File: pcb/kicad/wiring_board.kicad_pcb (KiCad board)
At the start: 2 copper layers, 47 x 72 mm, 13 parts, among them J1 2604-1106, J2 5V out

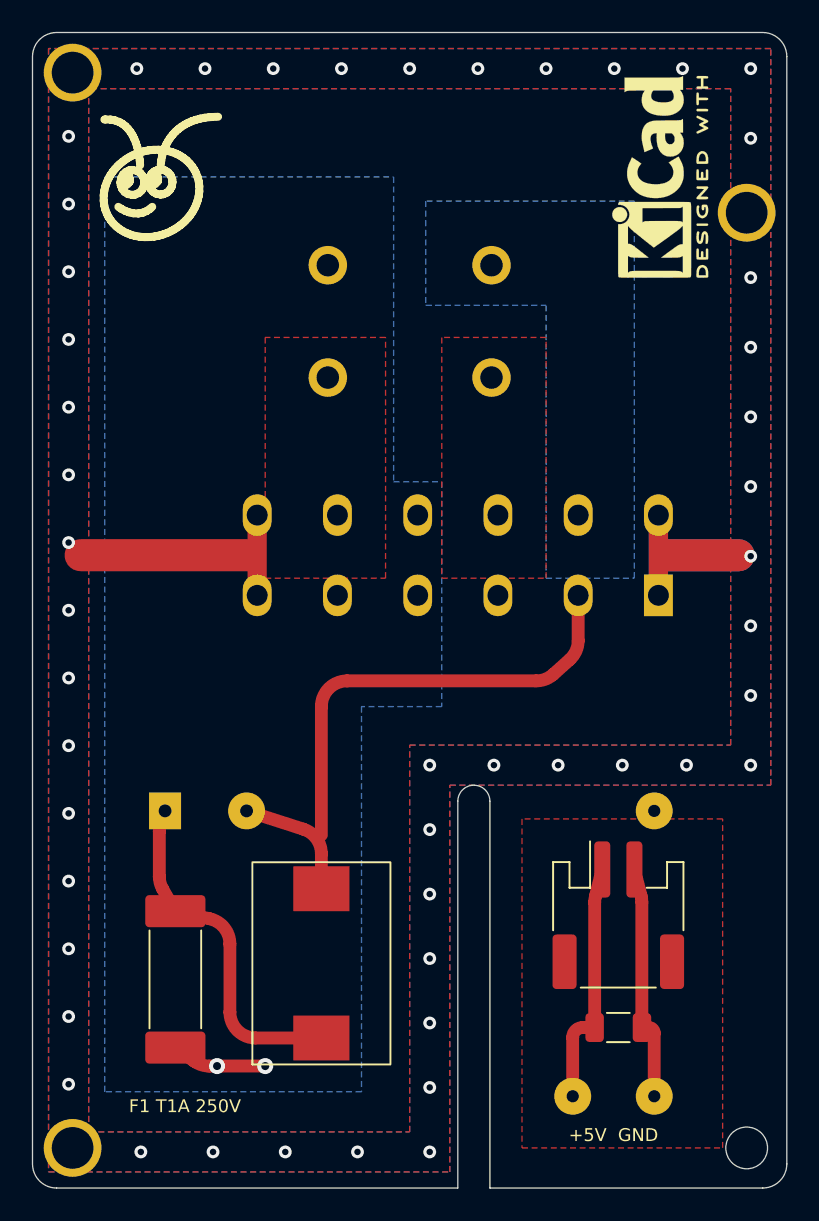
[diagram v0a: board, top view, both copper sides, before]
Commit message: Wiring board: J1 and rocker from vendor models, rocker clear of WAGO pins, LOAD labels
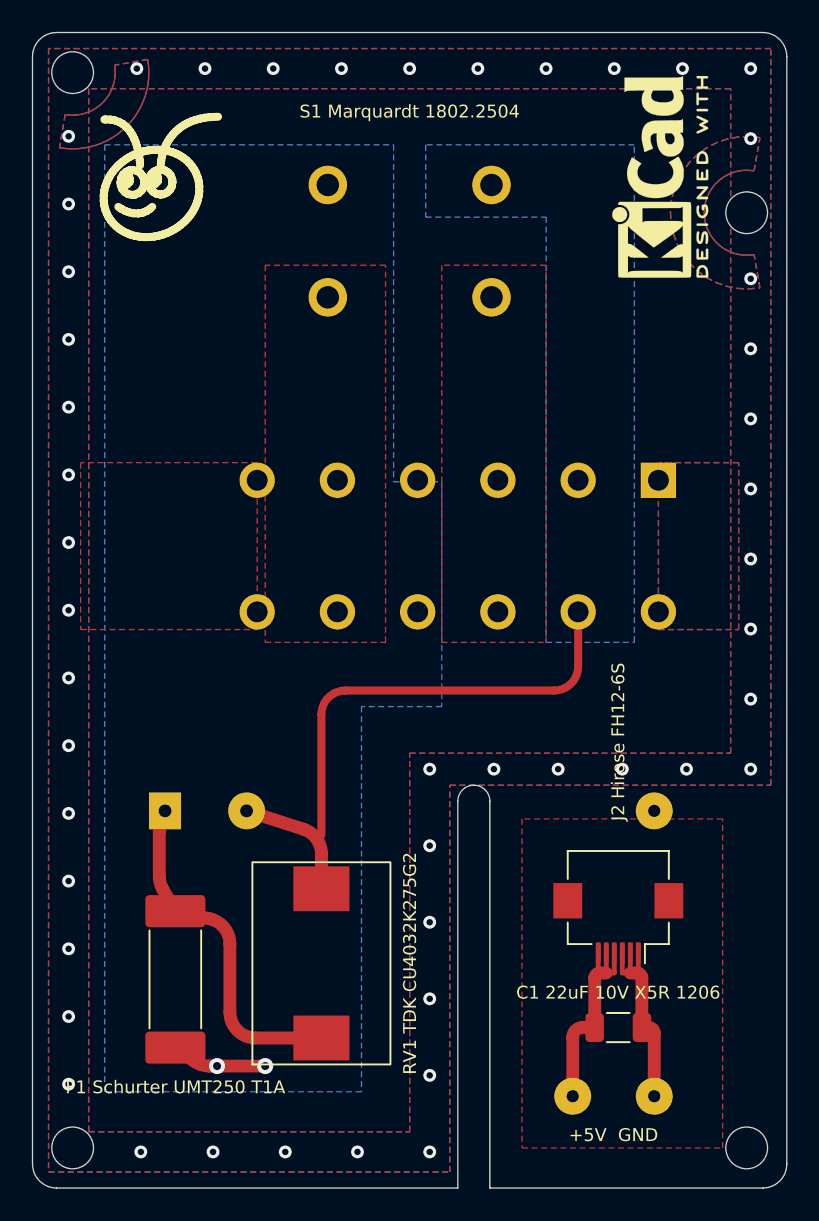
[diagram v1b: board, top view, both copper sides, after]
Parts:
- J2: value 5V out -> 5V out (flex jumper); footprint wiring_board:JST_PH_S2B-PH-SM4-TB_1x02-1MP_P2.00mm_Horizontal -> wiring_board:Hirose_FH12-6S-0.5SH_1x06-1MP_P0.50mm_Horizontal
- MH1, MH2, MH3: value MountingHole_2.6mm_Pad_PE -> MountingHole_2.6mm_NPTH; footprint wiring_board:MountingHole_2.6mm_Pad_PE -> wiring_board:MountingHole_2.6mm_NPTH
- moved J1 7.17 mm to (103.0, 91.9)
- moved S1 1.50 mm to (100.0, 80.5)
- moved J2 0.50 mm to (113.0, 119.5), turned to 180 degrees
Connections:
- J2 pad 1: +5V -> GND
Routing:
- net /PE: track 34.2 -> 0.00 mm, vias 49 -> 48
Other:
- board text added: "2026-10-09"
- board text added: "C1 22uF 10V X5R 1206"
- board text added: "F1 Schurter UMT250 T1A"
- board text added: "J1 WAGO 2604-1106"
- board text added: "J2 Hirose FH12-6S"
- board text added: "LOAD: L SW / N SW"
- board text added: "PS1 Mean Well IRM-03-5"
- board text added: "RV1 TDK CU4032K275G2"
- board text added: "S1 Marquardt 1802.2504"
- board text removed: "2026-10-07"
- board text removed: "F1 T1A 250V"
- board text removed: "LIGHTS: L SW / N SW"
